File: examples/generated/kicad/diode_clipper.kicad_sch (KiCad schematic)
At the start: 3 parts

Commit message: Attempt to create legible symbols.
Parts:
- D1: symbol examples:DIODE -> DIODE
- R1: symbol examples:R -> R
- V1: symbol examples:VSOURCE -> VSOURCE
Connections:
- net GND: now also D1.2 (A), V1.1 (E1)
- new net: R1.1, V1.2 (E2)
- new net: D1.1 (K), R1.2
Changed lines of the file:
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@@
     (comment 1 "Generated by mixedsig2cad")
   )
-  (symbol (lib_id "examples:VSOURCE") (at 50.00 55.00 0) (unit 1)
+  (symbol (lib_id "VSOURCE") (at 50.00 55.00 0) (unit 1)
     (in_bom yes) (on_board yes)
     (property "Reference" "V1" (at 50.0 51.19 0)
@@
     )
   )
-  (symbol (lib_id "examples:R") (at 95.00 55.00 90) (unit 1)
+  (symbol (lib_id "R") (at 95.00 55.00 90) (unit 1)
     (in_bom yes) (on_board yes)
     (property "Reference" "R1" (at 95.0 51.19 0)
@@
     )
   )
-  (symbol (lib_id "examples:DIODE") (at 95.00 90.00 0) (unit 1)
+  (symbol (lib_id "DIODE") (at 95.00 90.00 0) (unit 1)
     (in_bom yes) (on_board yes)
     (property "Reference" "D1" (at 95.0 86.19 0)
@@
     )
   )
-  (symbol (lib_id "examples:GND") (at 38.00 41.38 0) (unit 1)
+  (symbol (lib_id "GND") (at 38.00 41.38 0) (unit 1)
     (in_bom yes) (on_board yes)
     (property "Reference" "#PWR0001" (at 38.0 37.57 0)

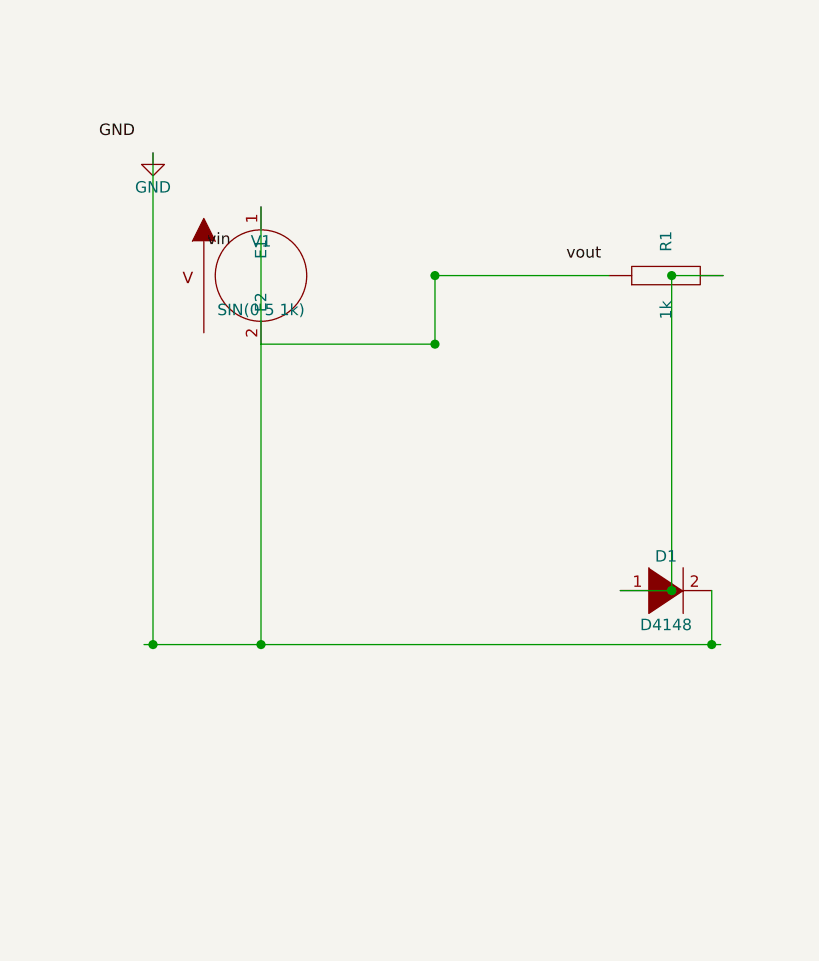
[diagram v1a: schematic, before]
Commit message: Attempt full seperation of circuit concerns into layers.
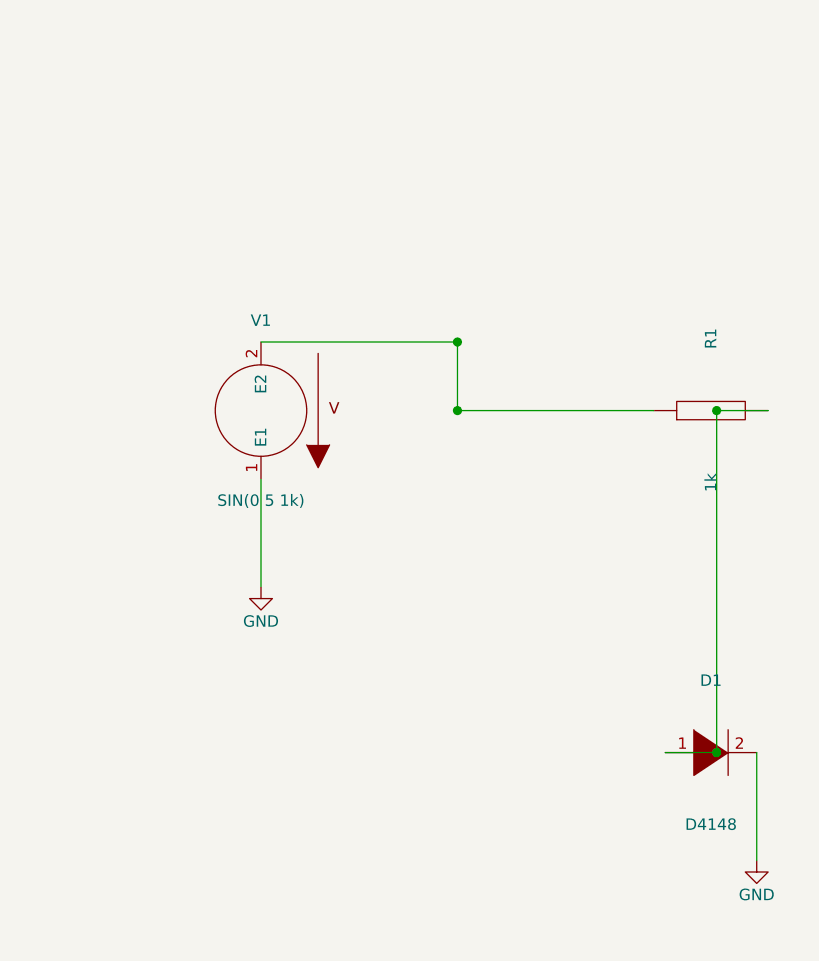
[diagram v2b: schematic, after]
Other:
- moved on the sheet: D1, R1, V1
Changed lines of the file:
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@@
   (title_block
     (title "diode_clipper")
-    (date "2026-03-05")
+    (date "2026-03-06")
     (comment 1 "Generated by mixedsig2cad")
   )
-  (symbol (lib_id "VSOURCE") (at 50.00 55.00 0) (unit 1)
+  (symbol (lib_id "VSOURCE") (at 50.00 70.00 180) (unit 1)
     (in_bom yes) (on_board yes)
-    (property "Reference" "V1" (at 50.0 51.19 0)
+    (property "Reference" "V1" (at 50.0 60.0 0)
       (effects (font (size 1.27 1.27)))
     )
-    (property "Value" "SIN(0 5 1k)" (at 50.0 58.81 0)
+    (property "Value" "SIN(0 5 1k)" (at 50.0 80.0 0)
       (effects (font (size 1.27 1.27)))
     )
@@
     )
   )
-  (symbol (lib_id "R") (at 95.00 55.00 90) (unit 1)
+  (symbol (lib_id "R") (at 100.00 70.00 90) (unit 1)
     (in_bom yes) (on_board yes)
-    (property "Reference" "R1" (at 95.0 51.19 0)
+    (property "Reference" "R1" (at 100.0 62.0 0)
       (effects (font (size 1.27 1.27)))
     )
-    (property "Value" "1k" (at 95.0 58.81 0)
+    (property "Value" "1k" (at 100.0 78.0 0)
       (effects (font (size 1.27 1.27)))
     )
@@
     )
   )
-  (symbol (lib_id "DIODE") (at 95.00 90.00 0) (unit 1)
+  (symbol (lib_id "DIODE") (at 100.00 108.00 0) (unit 1)
     (in_bom yes) (on_board yes)
-    (property "Reference" "D1" (at 95.0 86.19 0)
+    (property "Reference" "D1" (at 100.0 100.0 0)
       (effects (font (size 1.27 1.27)))
     )
-    (property "Value" "D4148" (at 95.0 93.81 0)
+    (property "Value" "D4148" (at 100.0 116.0 0)
       (effects (font (size 1.27 1.27)))
     )
@@
     )
   )
-  (symbol (lib_id "GND") (at 38.00 41.38 0) (unit 1)
+  (symbol (lib_id "GND") (at 50.00 89.62 0) (unit 1)
     (in_bom yes) (on_board yes)
-    (property "Reference" "#PWR0001" (at 38.0 37.57 0)
+    (property "Reference" "#PWR0001" (at 50.0 85.81 0)
       (effects (font (size 1.27 1.27)) hide)
     )
-    (property "Value" "GND" (at 38.0 45.190000000000005 0)
+    (property "Value" "GND" (at 50.0 93.43 0)
       (effects (font (size 1.27 1.27)))
     )
@@
     )
   )
-  (label "GND" (at 32.00 39.88 0)
-    (effects (font (size 1.27 1.27)) (justify left bottom))
+  (symbol (lib_id "GND") (at 105.08 120.00 0) (unit 1)
+    (in_bom yes) (on_board yes)
+    (property "Reference" "#PWR0002" (at 105.08 116.19 0)
+      (effects (font (size 1.27 1.27)) hide)
+    )
+    (property "Value" "GND" (at 105.08 123.81 0)
+      (effects (font (size 1.27 1.27)))
+    )
+    (property "Footprint" "" (at 0 0 0)
+      (effects (font (size 1.27 1.27)) hide)
+    )
+    (property "Datasheet" "" (at 0 0 0)
+      (effects (font (size 1.27 1.27)) hide)
+    )
   )
-  (label "vin" (at 44.00 52.00 0)
-    (effects (font (size 1.27 1.27)) (justify left bottom))
-  )
-  (label "vout" (at 83.92 53.50 0)
-    (effects (font (size 1.27 1.27)) (justify left bottom))
-  )
-  (wire (pts (xy 37.00 96.00) (xy 101.08 96.00))
+  (wire (pts (xy 50.00 77.62) (xy 50.00 89.62))
     (stroke (width 0) (type solid) (color 0 0 0 0))
   )
-  (wire (pts (xy 50.00 47.38) (xy 50.00 96.00))
+  (wire (pts (xy 105.08 108.00) (xy 105.08 120.00))
     (stroke (width 0) (type solid) (color 0 0 0 0))
   )
-  (wire (pts (xy 100.08 90.00) (xy 100.08 96.00))
+  (wire (pts (xy 50.00 62.38) (xy 71.83 62.38))
     (stroke (width 0) (type solid) (color 0 0 0 0))
   )
-  (wire (pts (xy 38.00 41.38) (xy 38.00 96.00))
+  (wire (pts (xy 71.83 62.38) (xy 71.83 70.00))
     (stroke (width 0) (type solid) (color 0 0 0 0))
   )
-  (wire (pts (xy 50.00 62.62) (xy 69.33 62.62))
+  (wire (pts (xy 71.83 70.00) (xy 93.65 70.00))
     (stroke (width 0) (type solid) (color 0 0 0 0))
   )
-  (wire (pts (xy 69.33 62.62) (xy 69.33 55.00))
+  (wire (pts (xy 106.35 70.00) (xy 100.63 70.00))
     (stroke (width 0) (type solid) (color 0 0 0 0))
   )
-  (wire (pts (xy 69.33 55.00) (xy 88.65 55.00))
+  (wire (pts (xy 100.63 70.00) (xy 100.63 108.00))
     (stroke (width 0) (type solid) (color 0 0 0 0))
   )
-  (wire (pts (xy 101.35 55.00) (xy 95.63 55.00))
+  (wire (pts (xy 100.63 108.00) (xy 94.92 108.00))
     (stroke (width 0) (type solid) (color 0 0 0 0))
   )
-  (wire (pts (xy 95.63 55.00) (xy 95.63 90.00))
-    (stroke (width 0) (type solid) (color 0 0 0 0))
-  )
-  (wire (pts (xy 95.63 90.00) (xy 89.92 90.00))
-    (stroke (width 0) (type solid) (color 0 0 0 0))
-  )
-  (junction (at 50.00 96.00) (diameter 1.016) (color 0 0 0 0))
-  (junction (at 100.08 96.00) (diameter 1.016) (color 0 0 0 0))
-  (junction (at 38.00 96.00) (diameter 1.016) (color 0 0 0 0))
-  (junction (at 69.33 62.62) (diameter 1.016) (color 0 0 0 0))
-  (junction (at 69.33 55.00) (diameter 1.016) (color 0 0 0 0))
-  (junction (at 95.63 55.00) (diameter 1.016) (color 0 0 0 0))
-  (junction (at 95.63 90.00) (diameter 1.016) (color 0 0 0 0))
+  (junction (at 71.83 62.38) (diameter 1.016) (color 0 0 0 0))
+  (junction (at 71.83 70.00) (diameter 1.016) (color 0 0 0 0))
+  (junction (at 100.63 70.00) (diameter 1.016) (color 0 0 0 0))
+  (junction (at 100.63 108.00) (diameter 1.016) (color 0 0 0 0))
   (sheet_instances
     (path "/" (page "1"))
@@
     (path "/2c8aff2b-0935-51d8-b11f-1b19ccafeed0" (reference "R1") (unit 1) (value "1k") (footprint ""))
     (path "/6d337348-46f7-501d-8787-9fc457eabff9" (reference "D1") (unit 1) (value "D4148") (footprint ""))
-    (path "/2f0f1d9e-453e-5c92-8e03-d3a9386a5af0" (reference "#PWR0001") (unit 1) (value "GND") (footprint ""))
+    (path "/229331e1-49b2-5d63-84c6-e3f127e9d83d" (reference "#PWR0001") (unit 1) (value "GND") (footprint ""))
+    (path "/331ec4ee-80da-5867-9867-b03498e7d5de" (reference "#PWR0002") (unit 1) (value "GND") (footprint ""))
   )
 )

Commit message: Add checks for connectivity.
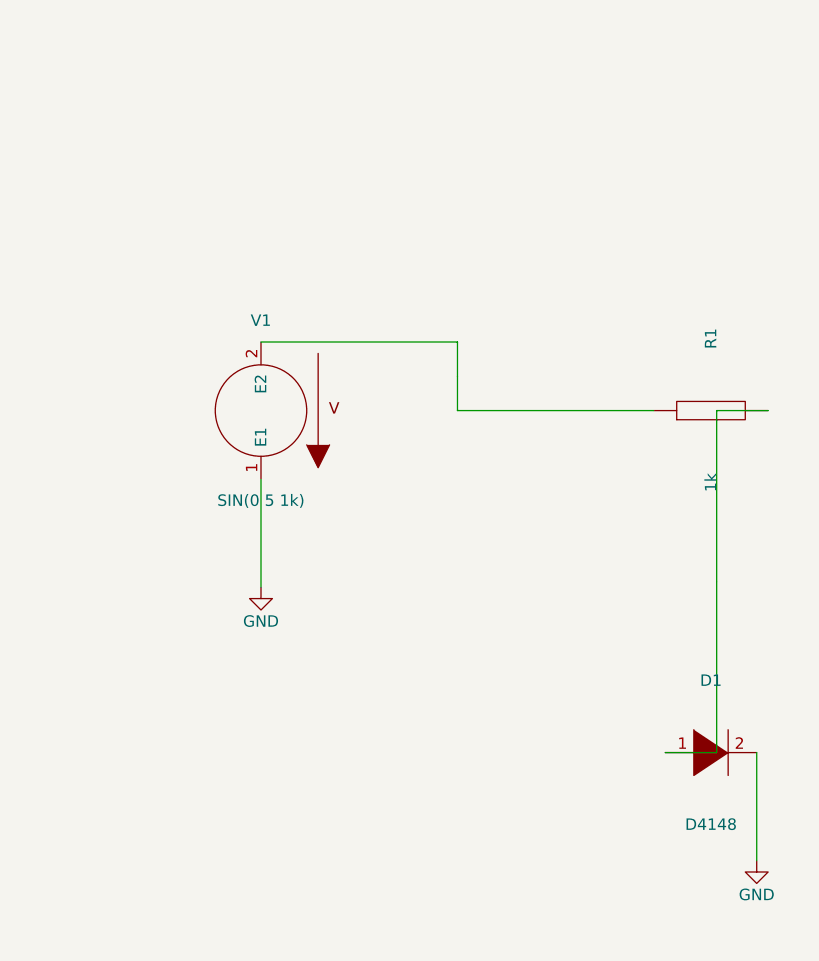
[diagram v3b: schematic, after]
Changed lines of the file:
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@@
     (stroke (width 0) (type solid) (color 0 0 0 0))
   )
-  (wire (pts (xy 71.83 62.38) (xy 71.83 70.00))
+  (wire (pts (xy 71.83 62.38) (xy 71.83 66.19))
     (stroke (width 0) (type solid) (color 0 0 0 0))
   )
-  (wire (pts (xy 71.83 70.00) (xy 93.65 70.00))
+  (wire (pts (xy 93.65 70.00) (xy 71.83 70.00))
+    (stroke (width 0) (type solid) (color 0 0 0 0))
+  )
+  (wire (pts (xy 71.83 70.00) (xy 71.83 66.19))
     (stroke (width 0) (type solid) (color 0 0 0 0))
   )
@@
     (stroke (width 0) (type solid) (color 0 0 0 0))
   )
-  (wire (pts (xy 100.63 70.00) (xy 100.63 108.00))
+  (wire (pts (xy 100.63 70.00) (xy 100.63 89.00))
     (stroke (width 0) (type solid) (color 0 0 0 0))
   )
-  (wire (pts (xy 100.63 108.00) (xy 94.92 108.00))
+  (wire (pts (xy 94.92 108.00) (xy 100.63 108.00))
     (stroke (width 0) (type solid) (color 0 0 0 0))
   )
-  (junction (at 71.83 62.38) (diameter 1.016) (color 0 0 0 0))
-  (junction (at 71.83 70.00) (diameter 1.016) (color 0 0 0 0))
-  (junction (at 100.63 70.00) (diameter 1.016) (color 0 0 0 0))
-  (junction (at 100.63 108.00) (diameter 1.016) (color 0 0 0 0))
+  (wire (pts (xy 100.63 108.00) (xy 100.63 89.00))
+    (stroke (width 0) (type solid) (color 0 0 0 0))
+  )
   (sheet_instances
     (path "/" (page "1"))

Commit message: Attempt to correct strange wiring.
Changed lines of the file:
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@@
     (stroke (width 0) (type solid) (color 0 0 0 0))
   )
-  (wire (pts (xy 50.00 62.38) (xy 71.83 62.38))
+  (wire (pts (xy 50.00 62.38) (xy 50.00 70.00))
     (stroke (width 0) (type solid) (color 0 0 0 0))
   )
-  (wire (pts (xy 71.83 62.38) (xy 71.83 66.19))
+  (wire (pts (xy 50.00 70.00) (xy 93.65 70.00))
     (stroke (width 0) (type solid) (color 0 0 0 0))
   )
-  (wire (pts (xy 93.65 70.00) (xy 71.83 70.00))
+  (wire (pts (xy 106.35 70.00) (xy 107.50 70.00))
     (stroke (width 0) (type solid) (color 0 0 0 0))
   )
-  (wire (pts (xy 71.83 70.00) (xy 71.83 66.19))
+  (wire (pts (xy 107.50 70.00) (xy 107.50 108.00))
     (stroke (width 0) (type solid) (color 0 0 0 0))
   )
-  (wire (pts (xy 106.35 70.00) (xy 100.63 70.00))
+  (wire (pts (xy 107.50 108.00) (xy 94.92 108.00))
     (stroke (width 0) (type solid) (color 0 0 0 0))
   )
-  (wire (pts (xy 100.63 70.00) (xy 100.63 89.00))
-    (stroke (width 0) (type solid) (color 0 0 0 0))
-  )
-  (wire (pts (xy 94.92 108.00) (xy 100.63 108.00))
-    (stroke (width 0) (type solid) (color 0 0 0 0))
-  )
-  (wire (pts (xy 100.63 108.00) (xy 100.63 89.00))
-    (stroke (width 0) (type solid) (color 0 0 0 0))
-  )

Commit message: Attempt shape and wiring fixes again.
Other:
- moved on the sheet: D1, R1, V1
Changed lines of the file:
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@@
     (comment 1 "Generated by mixedsig2cad")
   )
-  (symbol (lib_id "VSOURCE") (at 50.00 70.00 180) (unit 1)
+  (symbol (lib_id "VSOURCE") (at 56.00 86.00 180) (unit 1)
     (in_bom yes) (on_board yes)
-    (property "Reference" "V1" (at 50.0 60.0 0)
+    (property "Reference" "V1" (at 56.0 76.0 0)
       (effects (font (size 1.27 1.27)))
     )
-    (property "Value" "SIN(0 5 1k)" (at 50.0 80.0 0)
+    (property "Value" "SIN(0 5 1k)" (at 56.0 96.0 0)
       (effects (font (size 1.27 1.27)))
     )
@@
     )
   )
-  (symbol (lib_id "R") (at 100.00 70.00 90) (unit 1)
+  (symbol (lib_id "R") (at 90.00 78.00 90) (unit 1)
     (in_bom yes) (on_board yes)
-    (property "Reference" "R1" (at 100.0 62.0 0)
+    (property "Reference" "R1" (at 90.0 70.0 0)
       (effects (font (size 1.27 1.27)))
     )
-    (property "Value" "1k" (at 100.0 78.0 0)
+    (property "Value" "1k" (at 90.0 86.0 0)
       (effects (font (size 1.27 1.27)))
     )
@@
     )
   )
-  (symbol (lib_id "DIODE") (at 100.00 108.00 0) (unit 1)
+  (symbol (lib_id "DIODE") (at 90.00 112.00 0) (unit 1)
     (in_bom yes) (on_board yes)
-    (property "Reference" "D1" (at 100.0 100.0 0)
+    (property "Reference" "D1" (at 90.0 104.0 0)
       (effects (font (size 1.27 1.27)))
     )
-    (property "Value" "D4148" (at 100.0 116.0 0)
+    (property "Value" "D4148" (at 90.0 120.0 0)
       (effects (font (size 1.27 1.27)))
     )
@@
     )
   )
-  (symbol (lib_id "GND") (at 50.00 89.62 0) (unit 1)
+  (symbol (lib_id "GND") (at 56.00 105.62 0) (unit 1)
     (in_bom yes) (on_board yes)
-    (property "Reference" "#PWR0001" (at 50.0 85.81 0)
+    (property "Reference" "#PWR0001" (at 56.0 101.81 0)
       (effects (font (size 1.27 1.27)) hide)
     )
-    (property "Value" "GND" (at 50.0 93.43 0)
+    (property "Value" "GND" (at 56.0 109.43 0)
       (effects (font (size 1.27 1.27)))
     )
@@
     )
   )
-  (symbol (lib_id "GND") (at 105.08 120.00 0) (unit 1)
+  (symbol (lib_id "GND") (at 95.08 124.00 0) (unit 1)
     (in_bom yes) (on_board yes)
-    (property "Reference" "#PWR0002" (at 105.08 116.19 0)
+    (property "Reference" "#PWR0002" (at 95.08 120.19 0)
       (effects (font (size 1.27 1.27)) hide)
     )
-    (property "Value" "GND" (at 105.08 123.81 0)
+    (property "Value" "GND" (at 95.08 127.81 0)
       (effects (font (size 1.27 1.27)))
     )
@@
     )
   )
-  (wire (pts (xy 50.00 77.62) (xy 50.00 89.62))
+  (wire (pts (xy 56.00 93.62) (xy 56.00 95.50))
     (stroke (width 0) (type solid) (color 0 0 0 0))
   )
-  (wire (pts (xy 105.08 108.00) (xy 105.08 120.00))
+  (wire (pts (xy 56.00 95.50) (xy 62.00 95.50))
     (stroke (width 0) (type solid) (color 0 0 0 0))
   )
-  (wire (pts (xy 50.00 62.38) (xy 50.00 70.00))
+  (wire (pts (xy 62.00 95.50) (xy 62.00 105.62))
     (stroke (width 0) (type solid) (color 0 0 0 0))
   )
-  (wire (pts (xy 50.00 70.00) (xy 93.65 70.00))
+  (wire (pts (xy 62.00 105.62) (xy 56.00 105.62))
     (stroke (width 0) (type solid) (color 0 0 0 0))
   )
-  (wire (pts (xy 106.35 70.00) (xy 107.50 70.00))
+  (wire (pts (xy 95.08 112.00) (xy 101.08 112.00))
     (stroke (width 0) (type solid) (color 0 0 0 0))
   )
-  (wire (pts (xy 107.50 70.00) (xy 107.50 108.00))
+  (wire (pts (xy 101.08 112.00) (xy 101.08 124.00))
     (stroke (width 0) (type solid) (color 0 0 0 0))
   )
-  (wire (pts (xy 107.50 108.00) (xy 94.92 108.00))
+  (wire (pts (xy 101.08 124.00) (xy 95.08 124.00))
     (stroke (width 0) (type solid) (color 0 0 0 0))
   )
+  (wire (pts (xy 56.00 78.38) (xy 56.00 78.00))
+    (stroke (width 0) (type solid) (color 0 0 0 0))
+  )
+  (wire (pts (xy 56.00 78.00) (xy 83.65 78.00))
+    (stroke (width 0) (type solid) (color 0 0 0 0))
+  )
+  (wire (pts (xy 96.35 78.00) (xy 98.50 78.00))
+    (stroke (width 0) (type solid) (color 0 0 0 0))
+  )
+  (wire (pts (xy 98.50 78.00) (xy 98.50 105.00))
+    (stroke (width 0) (type solid) (color 0 0 0 0))
+  )
+  (wire (pts (xy 98.50 105.00) (xy 82.50 105.00))
+    (stroke (width 0) (type solid) (color 0 0 0 0))
+  )
+  (wire (pts (xy 82.50 105.00) (xy 82.50 112.00))
+    (stroke (width 0) (type solid) (color 0 0 0 0))
+  )
+  (wire (pts (xy 82.50 112.00) (xy 84.92 112.00))
+    (stroke (width 0) (type solid) (color 0 0 0 0))
+  )

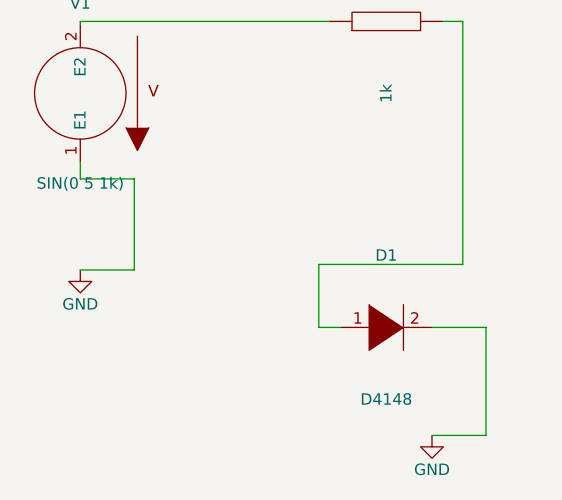
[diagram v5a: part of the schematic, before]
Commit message: Attempt to fix kinking and terminal direction issuses.
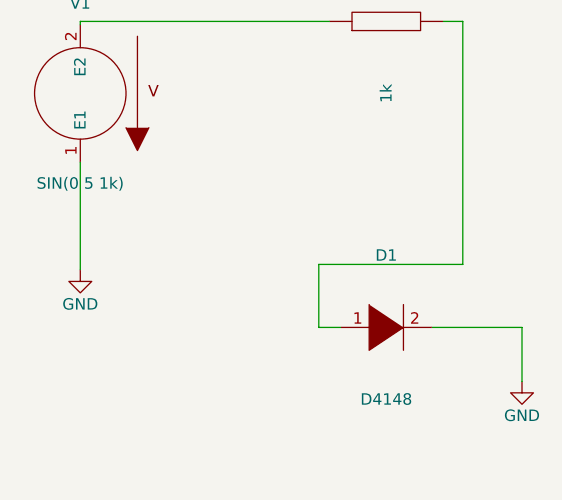
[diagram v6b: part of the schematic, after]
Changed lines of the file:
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@@
     )
   )
-  (symbol (lib_id "GND") (at 95.08 124.00 0) (unit 1)
+  (symbol (lib_id "GND") (at 105.08 118.00 0) (unit 1)
     (in_bom yes) (on_board yes)
-    (property "Reference" "#PWR0002" (at 95.08 120.19 0)
+    (property "Reference" "#PWR0002" (at 105.08 114.19 0)
       (effects (font (size 1.27 1.27)) hide)
     )
-    (property "Value" "GND" (at 95.08 127.81 0)
+    (property "Value" "GND" (at 105.08 121.81 0)
       (effects (font (size 1.27 1.27)))
     )
@@
     )
   )
-  (wire (pts (xy 56.00 93.62) (xy 56.00 95.50))
+  (wire (pts (xy 56.00 93.62) (xy 56.00 105.62))
     (stroke (width 0) (type solid) (color 0 0 0 0))
   )
-  (wire (pts (xy 56.00 95.50) (xy 62.00 95.50))
+  (wire (pts (xy 95.08 112.00) (xy 105.08 112.00))
     (stroke (width 0) (type solid) (color 0 0 0 0))
   )
-  (wire (pts (xy 62.00 95.50) (xy 62.00 105.62))
+  (wire (pts (xy 105.08 112.00) (xy 105.08 118.00))
     (stroke (width 0) (type solid) (color 0 0 0 0))
   )
-  (wire (pts (xy 62.00 105.62) (xy 56.00 105.62))
-    (stroke (width 0) (type solid) (color 0 0 0 0))
-  )
-  (wire (pts (xy 95.08 112.00) (xy 101.08 112.00))
-    (stroke (width 0) (type solid) (color 0 0 0 0))
-  )
-  (wire (pts (xy 101.08 112.00) (xy 101.08 124.00))
-    (stroke (width 0) (type solid) (color 0 0 0 0))
-  )
-  (wire (pts (xy 101.08 124.00) (xy 95.08 124.00))
-    (stroke (width 0) (type solid) (color 0 0 0 0))
-  )
